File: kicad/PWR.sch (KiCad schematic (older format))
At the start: 6 parts, among them J11 +12V GND -12V, U2 LM1117-5.0

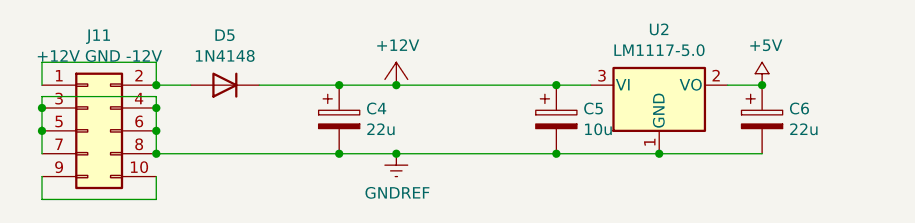
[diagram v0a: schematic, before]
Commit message: Use 6V. Add output diodes + output pin headers
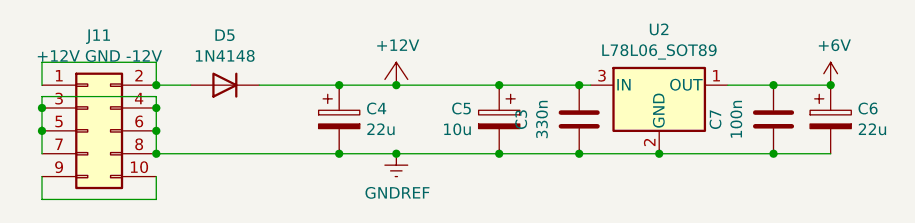
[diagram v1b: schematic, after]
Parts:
- removed U2: LM1117-5.0, Package_TO_SOT_SMD:SOT-223-3_TabPin2, symbol Regulator_Linear:LM1117-5.0
- added C3: 330n, Capacitor_SMD:C_0402_1005Metric, symbol Device:C
- added C7: 100n, Capacitor_SMD:C_0603_1608Metric, symbol Device:C
- added U2: L78L06_SOT89, Package_TO_SOT_SMD:SOT-89-3, symbol Regulator_Linear:L78L06_SOT89
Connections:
- net +12V: now also C3.2, U2.3 (IN)
- net GNDREF: now also C3.1, C7.1, U2.2 (GND)
- net +5V renamed +6V
- net +6V: now also C7.2, U2.1 (OUT)
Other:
- moved on the sheet: C5, C6
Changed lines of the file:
@@
 Connection ~ 2700 2000
-$Comp
-L Regulator_Linear:LM1117-5.0 U2
-U 1 1 5FF874F5
-P 4100 1700
-F 0 "U2" H 4100 1942 50  0000 C CNN
-F 1 "LM1117-5.0" H 4100 1851 50  0000 C CNN
-F 2 "Package_TO_SOT_SMD:SOT-223-3_TabPin2" H 4100 1700 50  0001 C CNN
-F 3 "http://www.ti.com/lit/ds/symlink/lm1117.pdf" H 4100 1700 50  0001 C CNN
-F 4 "C41202" H 4100 1700 50  0001 C CNN "LCSC"
-F 5 "926-LM1117IMPX50NOPB" H 4100 1700 50  0001 C CNN "mouser"
-	1    4100 1700
-	1    0    0    -1
-$EndComp
 $Comp
 L Device:CP C6
 U 1 1 5FF87FF0
-P 4550 1850
-F 0 "C6" H 4668 1896 50  0000 L CNN
-F 1 "22u" H 4668 1805 50  0000 L CNN
-F 2 "Capacitor_Tantalum_SMD:CP_EIA-3528-21_Kemet-B" H 4588 1700 50  0001 C CNN
-F 3 "https://datasheet.lcsc.com/szlcsc/AVX-TAJB226K016RNJ_C8020.pdf" H 4550 1850 50  0001 C CNN
-F 4 "C8020" H 4550 1850 50  0001 C CNN "LCSC"
-F 5 "581-TAJB226M016S" H 4550 1850 50  0001 C CNN "mouser"
-	1    4550 1850
+P 4850 1850
+F 0 "C6" H 4968 1896 50  0000 L CNN
+F 1 "22u" H 4968 1805 50  0000 L CNN
+F 2 "Capacitor_Tantalum_SMD:CP_EIA-3528-21_Kemet-B" H 4888 1700 50  0001 C CNN
+F 3 "https://datasheet.lcsc.com/szlcsc/AVX-TAJB226K016RNJ_C8020.pdf" H 4850 1850 50  0001 C CNN
+F 4 "C8020" H 4850 1850 50  0001 C CNN "LCSC"
+F 5 "581-TAJB226M016S" H 4850 1850 50  0001 C CNN "mouser"
+	1    4850 1850
 	1    0    0    -1
 $EndComp
@@
 L Device:CP C5
 U 1 1 5FF88826
-P 3650 1850
-F 0 "C5" H 3768 1896 50  0000 L CNN
-F 1 "10u" H 3768 1805 50  0000 L CNN
-F 2 "Capacitor_Tantalum_SMD:CP_EIA-6032-28_Kemet-C" H 3688 1700 50  0001 C CNN
-F 3 "https://datasheet.lcsc.com/szlcsc/KEMET-T491C106K025AT_C116748.pdf" H 3650 1850 50  0001 C CNN
-F 4 "C116748" H 3650 1850 50  0001 C CNN "LCSC"
-F 5 "80-T491C106K25AT7280" H 3650 1850 50  0001 C CNN "mouser"
-	1    3650 1850
-	1    0    0    -1
+P 3400 1850
+F 0 "C5" H 3518 1896 50  0000 L CNN
+F 1 "10u" H 3518 1805 50  0000 L CNN
+F 2 "Capacitor_Tantalum_SMD:CP_EIA-6032-28_Kemet-C" H 3438 1700 50  0001 C CNN
+F 3 "https://datasheet.lcsc.com/szlcsc/KEMET-T491C106K025AT_C116748.pdf" H 3400 1850 50  0001 C CNN
+F 4 "C116748" H 3400 1850 50  0001 C CNN "LCSC"
+F 5 "80-T491C106K25AT7280" H 3400 1850 50  0001 C CNN "mouser"
+	1    3400 1850
+	-1   0    0    -1
 $EndComp
+Connection ~ 2950 1700
 Wire Wire Line
-	3800 1700 3650 1700
-Connection ~ 2950 1700
-Connection ~ 3650 1700
-Wire Wire Line
-	3650 1700 2950 1700
-Wire Wire Line
-	2950 2000 3650 2000
+	2950 2000 3400 2000
 Connection ~ 2950 2000
-Connection ~ 3650 2000
-Wire Wire Line
-	3650 2000 4100 2000
-Connection ~ 4100 2000
-Wire Wire Line
-	4100 2000 4550 2000
-Wire Wire Line
-	4400 1700 4550 1700
 Wire Wire Line
 	1400 1800 1400 1750
@@
 Connection ~ 1400 1800
 Connection ~ 1900 1800
-$Comp
-L MySynthParts:+5V #PWR0134
-U 1 1 5FFD79AA
-P 4550 1700
-F 0 "#PWR0134" H 4550 1550 50  0001 C CNN
-F 1 "+5V" H 4565 1873 50  0000 C CNN
-F 2 "" H 4550 1700 60  0000 C CNN
-F 3 "" H 4550 1700 60  0000 C CNN
-	1    4550 1700
-	1    0    0    -1
-$EndComp
-Connection ~ 4550 1700
 Wire Wire Line
 	2350 1700 2700 1700
 Wire Wire Line
 	1900 2000 2700 2000
+$Comp
+L power:+6V #PWR?
+U 1 1 619C45D4
+P 4850 1700
+AR Path="/5FEC9095/619C45D4" Ref="#PWR?"  Part="1"
+AR Path="/5FEC8D3E/619C45D4" Ref="#PWR0120"  Part="1"
+F 0 "#PWR0120" H 4850 1550 50  0001 C CNN
+F 1 "+6V" H 4865 1873 50  0000 C CNN
+F 2 "" H 4850 1700 50  0001 C CNN
+F 3 "" H 4850 1700 50  0001 C CNN
+	1    4850 1700
+	1    0    0    -1
+$EndComp
+$Comp
+L Device:C C?
+U 1 1 619C5B42
+P 3750 1850
+AR Path="/5FEC8E2F/619C5B42" Ref="C?"  Part="1"
+AR Path="/5FEC8D3E/619C5B42" Ref="C3"  Part="1"
+F 0 "C3" V 4002 1850 50  0000 C CNN
+F 1 "330n" V 3911 1850 50  0000 C CNN
+F 2 "Capacitor_SMD:C_0402_1005Metric" H 3788 1700 50  0001 C CNN
+F 3 "https://datasheet.lcsc.com/lcsc/1810192025_Samsung-Electro-Mechanics-CL05C331JB5NNNC_C13533.pdf" H 3750 1850 50  0001 C CNN
+F 4 "C13533" H 3750 1850 50  0001 C CNN "LCSC"
+F 5 "581-06031C104KAT4A" H 3750 1850 50  0001 C CNN "mouser"
+	1    3750 1850
+	-1   0    0    1
+$EndComp
+Connection ~ 3400 1700
+Wire Wire Line
+	3400 1700 2950 1700
+Connection ~ 3400 2000
+Connection ~ 3750 1700
+Wire Wire Line
+	3750 1700 3800 1700
+Connection ~ 3750 2000
+Wire Wire Line
+	3400 1700 3750 1700
+Wire Wire Line
+	3400 2000 3750 2000
+$Comp
+L Device:C C?
+U 1 1 619C7F71
+P 4600 1850
+AR Path="/5FEC8E2F/619C7F71" Ref="C?"  Part="1"
+AR Path="/5FEC8D3E/619C7F71" Ref="C7"  Part="1"
+F 0 "C7" V 4852 1850 50  0000 C CNN
+F 1 "100n" V 4761 1850 50  0000 C CNN
+F 2 "Capacitor_SMD:C_0603_1608Metric" H 4638 1700 50  0001 C CNN
+F 3 "https://datasheet.lcsc.com/szlcsc/YAGEO-CC0603KRX7R9BB104_C14663.pdf" H 4600 1850 50  0001 C CNN
+F 4 "C14663" H 4600 1850 50  0001 C CNN "LCSC"
+F 5 "581-06031C104KAT4A" H 4600 1850 50  0001 C CNN "mouser"
+	1    4600 1850
+	-1   0    0    1
+$EndComp
+Connection ~ 4600 1700
+Wire Wire Line
+	4600 1700 4850 1700
+Connection ~ 4600 2000
+Wire Wire Line
+	4600 2000 4850 2000
+Connection ~ 4850 1700
+Wire Wire Line
+	4400 1700 4600 1700
+$Comp
+L Regulator_Linear:L78L06_SOT89 U2
+U 1 1 619CA752
+P 4100 1700
+F 0 "U2" H 4100 1942 50  0000 C CNN
+F 1 "L78L06_SOT89" H 4100 1851 50  0000 C CNN
+F 2 "Package_TO_SOT_SMD:SOT-89-3" H 4100 1900 50  0001 C CIN
+F 3 "http://www.st.com/content/ccc/resource/technical/document/datasheet/15/55/e5/aa/23/5b/43/fd/CD00000446.pdf/files/CD00000446.pdf/jcr:content/translations/en.CD00000446.pdf" H 4100 1650 50  0001 C CNN
+F 4 "C347269" H 4100 1700 50  0001 C CNN "LCSC"
+	1    4100 1700
+	1    0    0    -1
+$EndComp
+Wire Wire Line
+	3750 2000 4100 2000
+Connection ~ 4100 2000
+Wire Wire Line
+	4100 2000 4600 2000
 $EndSCHEMATC
